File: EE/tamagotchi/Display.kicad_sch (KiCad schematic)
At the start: 26 parts, among them J3 Conn_01x07, Q1 Q_NMOS_GSD, Q2 Q_NMOS_GSD

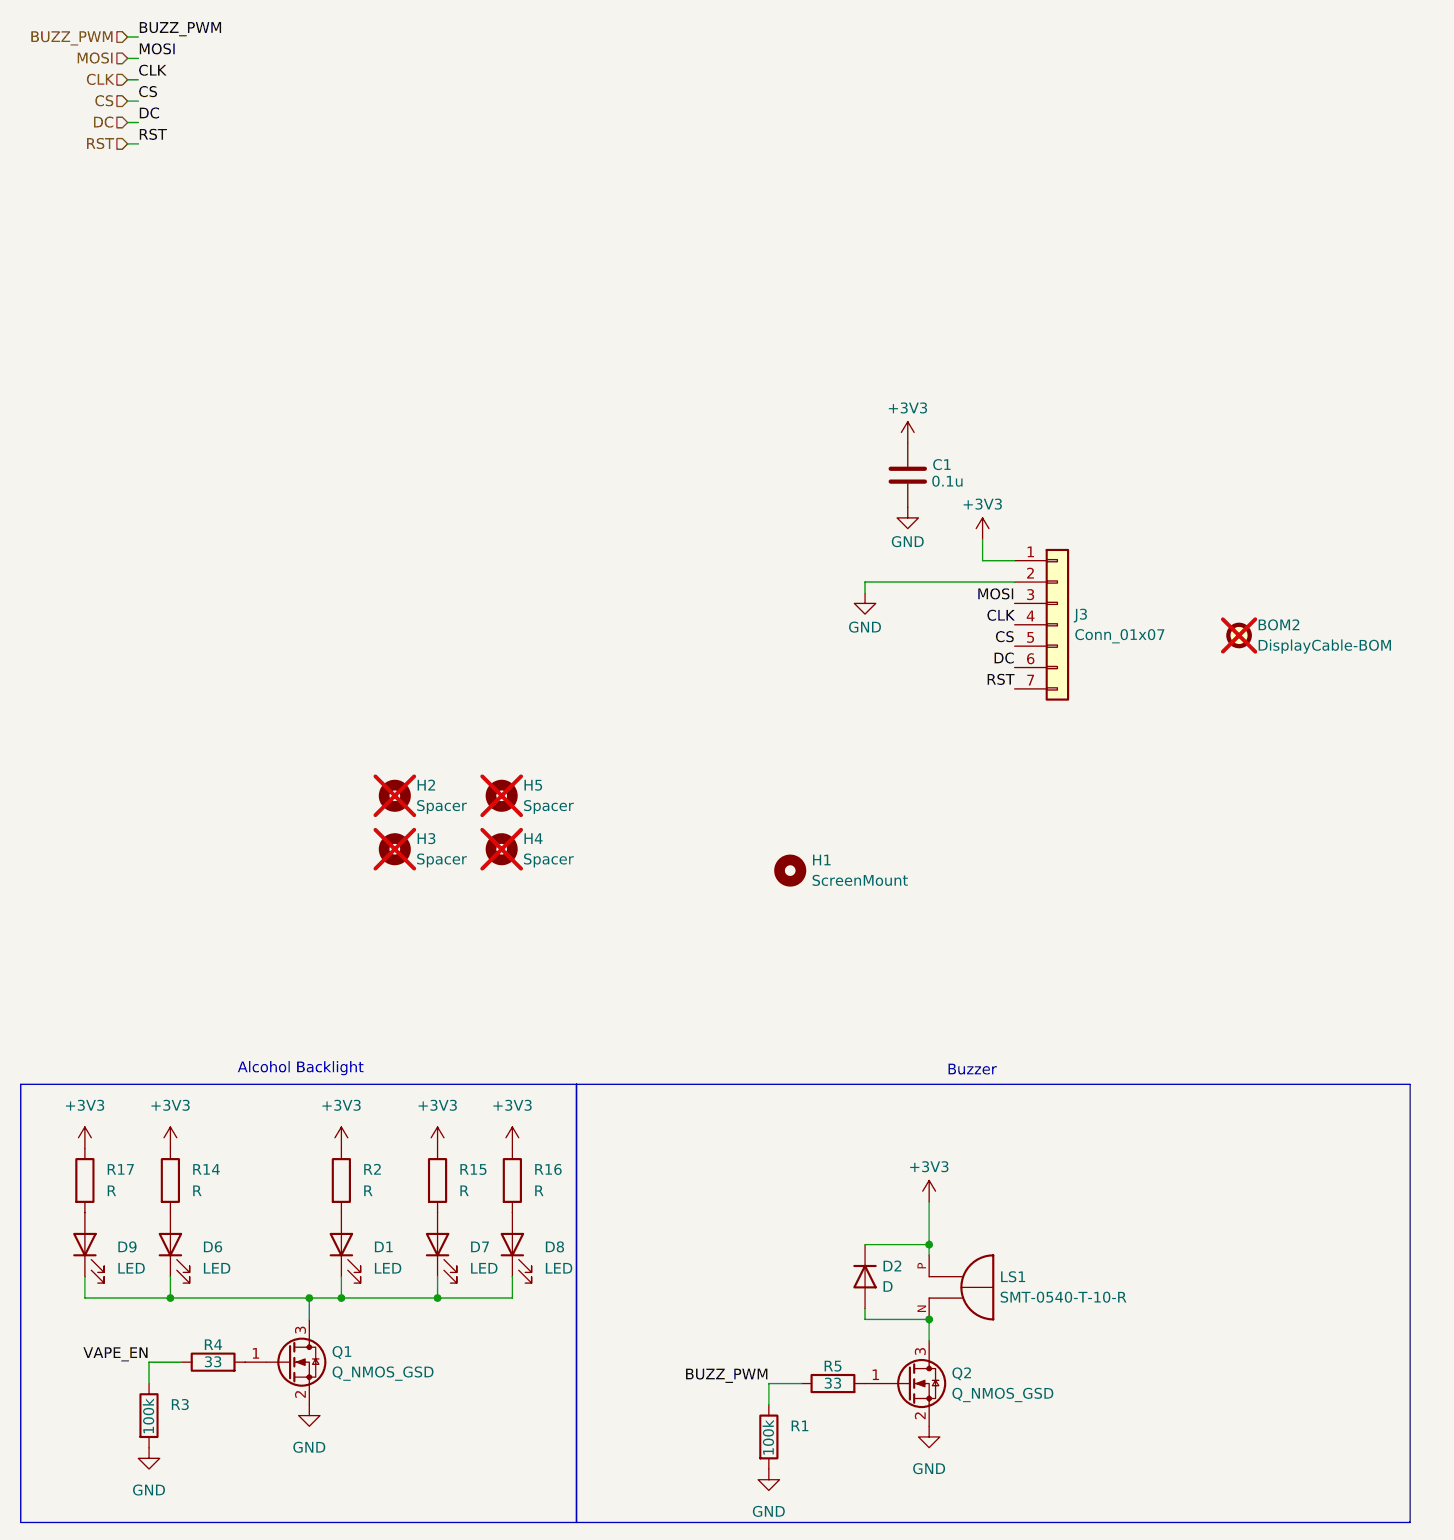
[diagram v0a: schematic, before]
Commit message: WIP - Overall Cleanup, Power Change
Added expected loads for power in schematic.
Changed power arch to use existing design that appears to work.
Removed rear backlight LEDs - shouldn't be necessary.
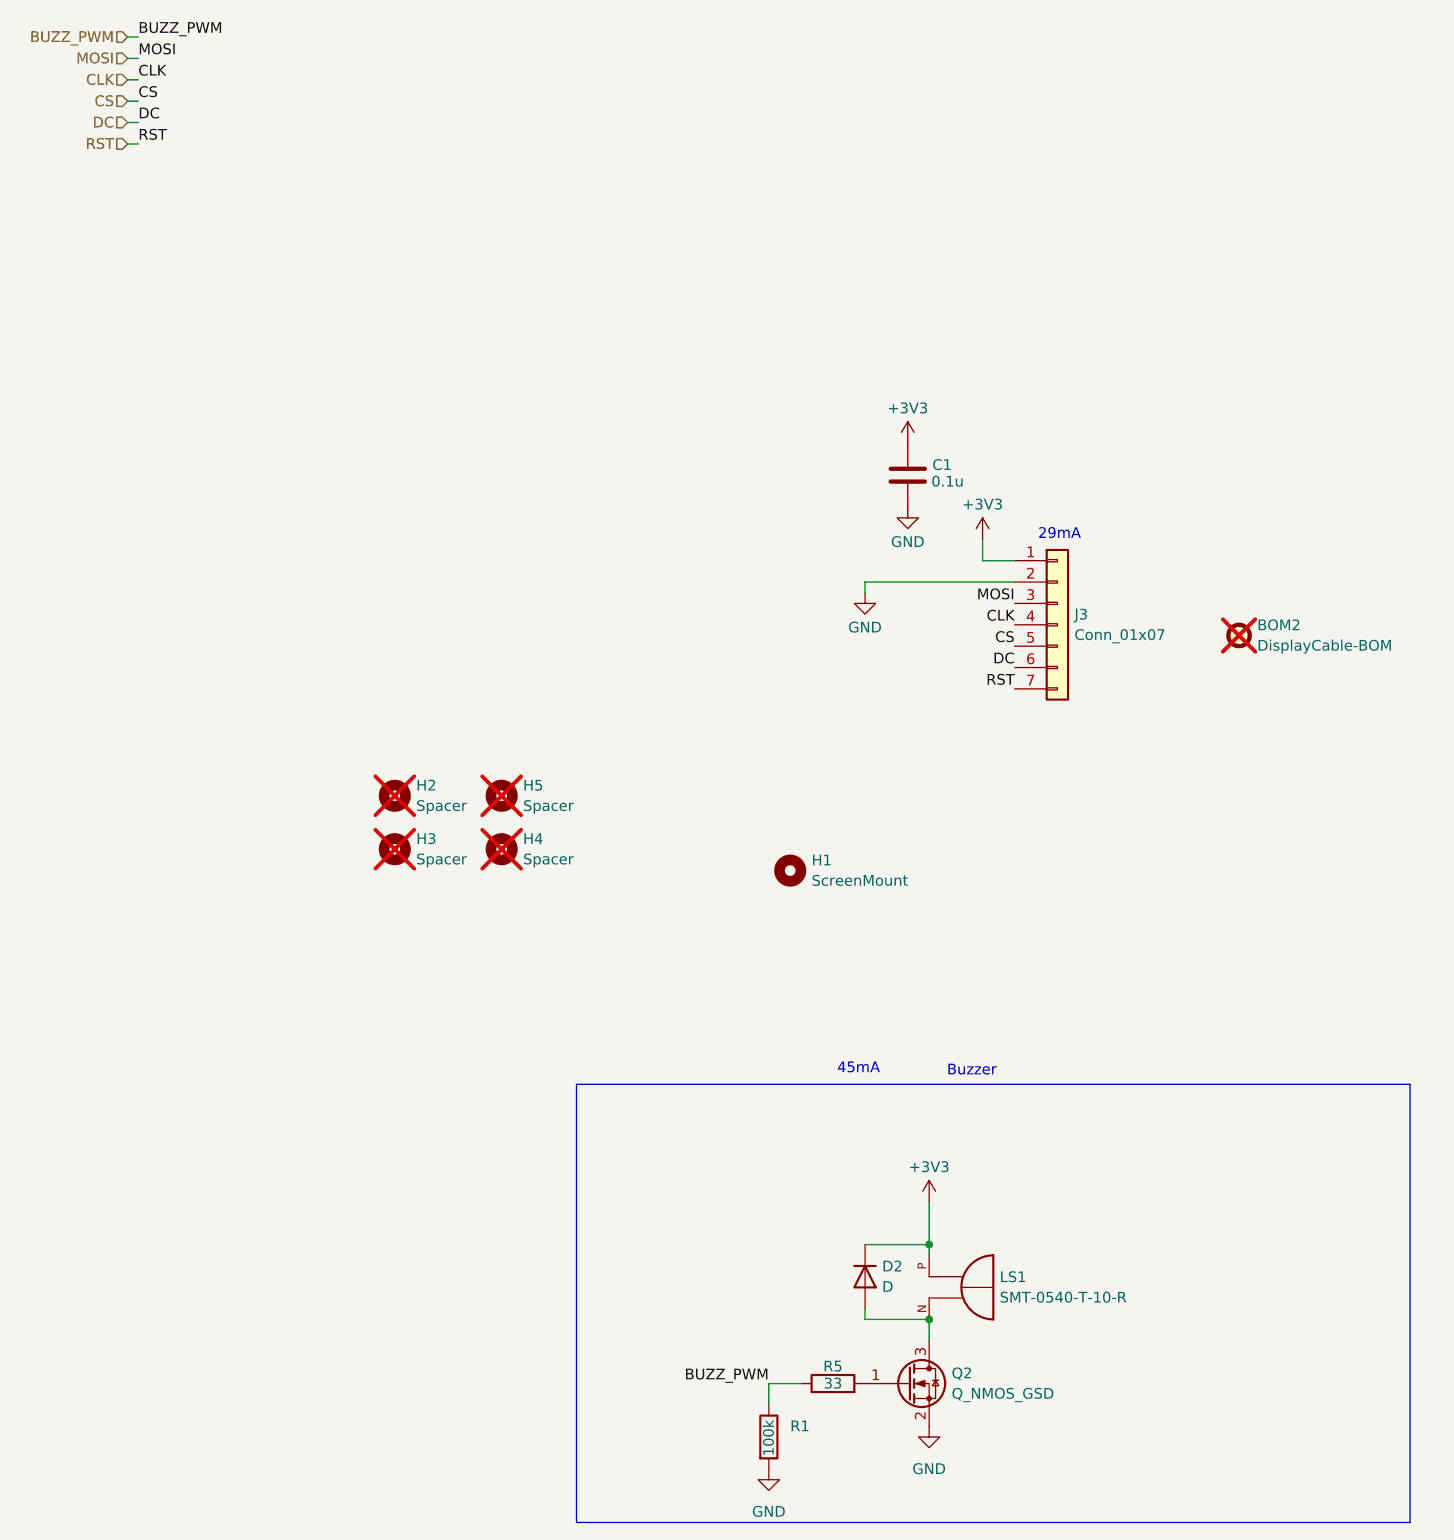
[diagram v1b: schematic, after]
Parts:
- removed D1, D6, D7, D8, D9: LED, LED_SMD:LED_0603_1608Metric_Pad1.05x0.95mm_HandSolder, symbol Device:LED
- removed Q1: Q_NMOS_GSD, Package_TO_SOT_SMD:SOT-23, symbol Transistor_FET:Q_NMOS_GSD
- removed R14, R15, R16, R17, R2: R, Resistor_SMD:R_0402_1005Metric_Pad0.72x0.64mm_HandSolder, symbol Device:R
- removed R3: 100k, Resistor_SMD:R_0402_1005Metric_Pad0.72x0.64mm_HandSolder, symbol Device:R
- removed R4: 33, Resistor_SMD:R_0402_1005Metric_Pad0.72x0.64mm_HandSolder, symbol Device:R
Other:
- note added: "29mA"
- note added: "45mA"
- note removed: "Alcohol Backlight"
